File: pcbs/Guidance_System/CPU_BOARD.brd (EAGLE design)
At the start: 100 x 80 mm, 16 parts, among them J1 22-27-2081-08, J2 22-27-2021-02, J3 22-05-7048-04, J4 22-05-7048-04, J5 22-27-2081-08, J6 22-27-2021-02, J7 22-27-2081-08

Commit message: * Added Driver board. Many corrections and refinements.
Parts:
- removed S1: 2P2T, switch:2P2T
- added J10, J11, J12, J13, J14: 22-27-2081-08, con-molex:6410-08
- added J15, J16: 22-27-2041-04, con-molex:6410-04
- added J17, J8, J9: 22-27-2021-02, con-molex:6410-02
- J3, J4: value 22-05-7048-04 -> 22-27-2041-04; device con-molex:7395-04 -> con-molex:6410-04
- moved J7 48.1 mm to (88.9, 33.0), turned to 0 degrees
- moved R6 28.4 mm to (92.7, 29.2)
- moved J5 19.1 mm to (59.7, 40.6), turned to 270 degrees
- moved J2 18.2 mm to (66.0, 66.0)
- moved J1 18.0 mm to (59.7, 62.2)
- moved R2 16.7 mm to (80.0, 62.2)
- moved R3 16.7 mm to (80.0, 59.7)
- moved U$1 16.7 mm to (77.5, 57.1)
- moved R4 15.9 mm to (95.2, 39.4), turned to 180 degrees
- moved LED1 13.1 mm to (66.0, 31.8)
- moved J6 11.7 mm to (72.4, 31.8), turned to 0 degrees
- moved R1 11.5 mm to (90.2, 62.2), turned to 90 degrees
- moved J3 10.2 mm to (95.2, 61.0)
- moved J4 9.67 mm to (95.2, 47.0)
- moved R5 8.89 mm to (66.0, 50.8)
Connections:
- new net N$19: J13.5, J13.6
- new net N$24: J1.1, J3.2, J4.2, J9.1, U$1.23
- new net N$26: J10.8, J14.8
- new net N$27: J10.7, J14.5
- new net N$28: J13.7, J14.6
- new net N$29: J13.8, J14.7
- new net N$31: J11.8, J12.8, J17.2
- new net N$32: J10.3, J11.2, J12.2, J13.3, J14.1
- new net N$33: J11.1, J12.1, J14.2
- new net N$34: J11.7, J12.7, J17.1
- new net N$35: J10.1, J13.1, J14.4
- new net N$37: J11.6, J15.1
- new net N$38: J11.5, J15.2
- new net N$39: J11.4, J15.3
- new net N$40: J11.3, J15.4
- new net N$41: J12.6, J16.1
- new net N$42: J12.5, J16.2
- new net N$43: J12.4, J16.3
- new net N$44: J12.3, J16.4
- net N$4: now also J10.5, J10.6; no longer J1.1, J3.2, J4.2, U$1.23
- net N$5: now also J8.2; no longer S1.3.2
- net VCC: now also J8.1, J9.2; no longer S1.3.1
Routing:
- net N$33: track 0.00 -> 129.5 mm, vias 0 -> 2
- net N$4: track 102.9 -> 2.54 mm
- net N$24: track 0.00 -> 99.1 mm
- net N$32: track 0.00 -> 98.3 mm, vias 0 -> 2
- net N$31: track 0.00 -> 47.0 mm
- net N$35: track 0.00 -> 46.6 mm
- net N$34: track 0.00 -> 41.9 mm, vias 0 -> 2
- net N$13: track 16.1 -> 56.7 mm
- net N$29: track 0.00 -> 36.8 mm
- net N$3: track 191.2 -> 156.1 mm
- net N$27: track 0.00 -> 33.0 mm, vias 0 -> 1
- net N$8: track 12.5 -> 42.4 mm
- net N$14: track 19.7 -> 47.5 mm
- net N$7: track 8.15 -> 35.6 mm
- net N$22: track 11.4 -> 35.3 mm
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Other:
- board size 100 x 80 mm -> 100 x 55.9 mm
- board text added: "S1 Driver"
- board text added: "S2 Driver"

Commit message: * Committing latest version before major shrinkage of boards
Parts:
- moved R6 6.84 mm to (86.4, 31.8)
- moved R5 4.58 mm to (62.2, 53.3)
- moved LED1 4.58 mm to (62.2, 34.3)
- moved J8 4.58 mm to (86.4, 72.4)
- moved J9 4.58 mm to (92.7, 72.4)
- moved J2 4.58 mm to (62.2, 68.6)
- moved J3 4.58 mm to (91.4, 63.5)
- moved J4 4.58 mm to (91.4, 49.5)
- moved J6 4.58 mm to (68.6, 34.3)
- moved J7 4.58 mm to (85.1, 35.6)
- moved R1 4.58 mm to (86.4, 64.8)
- moved R2 4.58 mm to (76.2, 64.8)
- moved R3 4.58 mm to (76.2, 62.2)
- moved R4 4.58 mm to (91.4, 41.9)
- moved U$1 4.58 mm to (73.7, 59.7)
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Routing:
- net N$3: track 156.1 -> 152.3 mm
- net N$27: track 33.0 -> 29.2 mm
- net N$29: track 36.8 -> 33.0 mm
- net N$17: track 46.5 -> 43.6 mm
- net N$24: track 99.1 -> 96.5 mm
- net N$22: track 35.3 -> 33.4 mm
- net N$26: track 15.2 -> 14.0 mm
- net N$33: track 129.5 -> 128.3 mm
- net N$32: track 98.3 -> 97.0 mm
- net N$21: track 32.8 -> 31.7 mm
- net GND: track 79.8 -> 78.8 mm
- net N$35: track 46.6 -> 47.5 mm
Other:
- board size 100 x 55.9 mm -> 100 x 49.5 mm

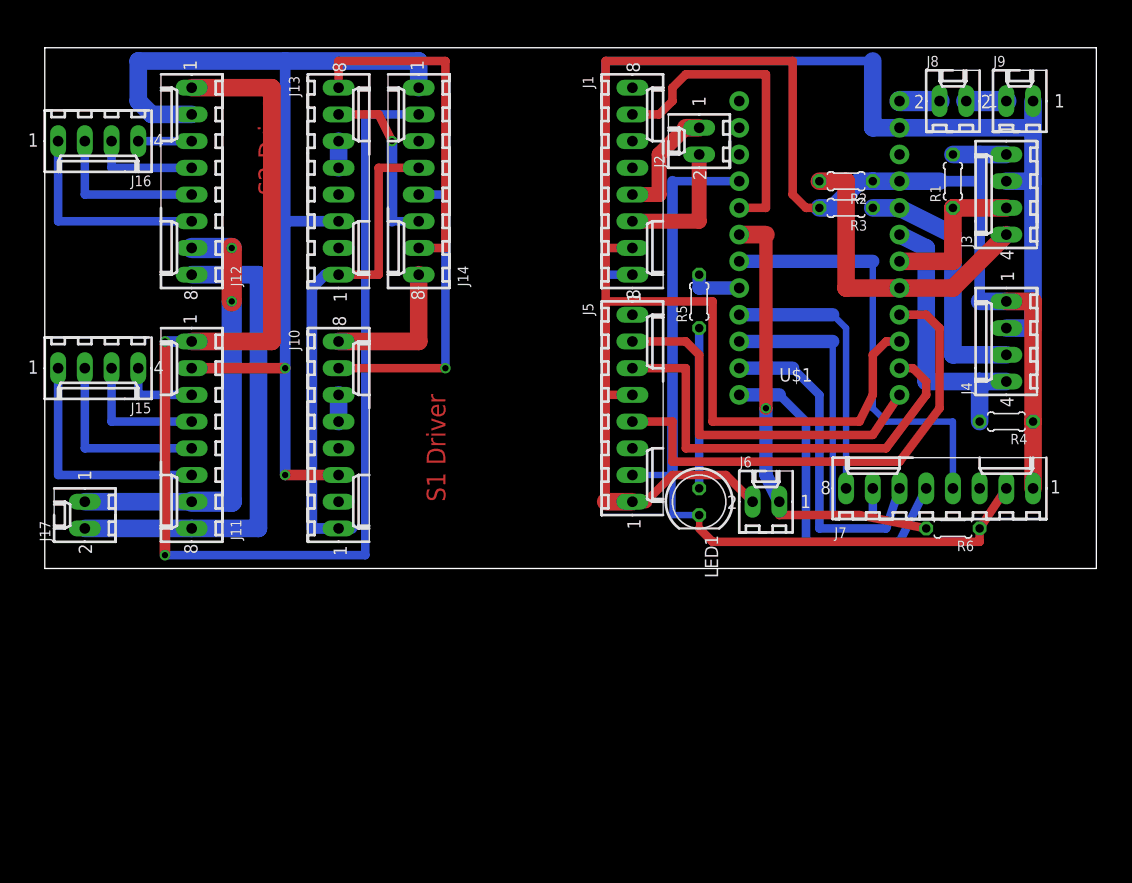
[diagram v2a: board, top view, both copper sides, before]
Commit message: * Made boards a lot smaller a much better layout!
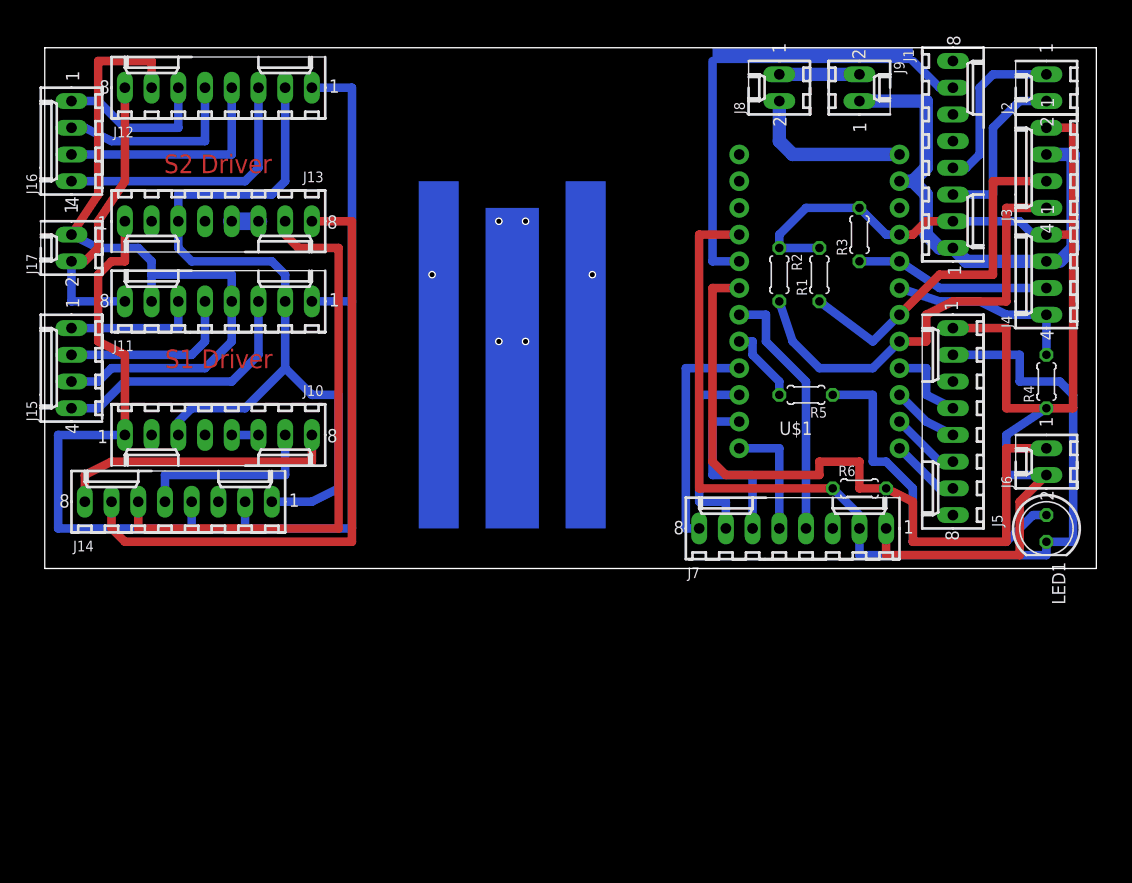
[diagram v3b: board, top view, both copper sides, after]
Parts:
- moved J14 38.1 mm to (12.7, 34.3), turned to 0 degrees
- moved J2 33.4 mm to (95.2, 73.7)
- moved LED1 33.1 mm to (95.2, 31.8)
- moved J1 30.6 mm to (86.4, 67.3)
- moved J5 30.5 mm to (86.4, 41.9), turned to 90 degrees
- moved J6 26.9 mm to (95.2, 38.1), turned to 90 degrees
- moved J17 25.4 mm to (2.54, 58.4)
- moved J8 16.6 mm to (69.8, 73.7), turned to 90 degrees
- moved R1 15.5 mm to (73.7, 55.9)
- moved J9 15.3 mm to (77.5, 73.7), turned to 270 degrees
- moved J7 14.5 mm to (71.1, 31.8)
- moved R5 13.5 mm to (72.4, 44.5), turned to 180 degrees
- moved J11 13.0 mm to (16.5, 53.3), turned to 0 degrees
- moved J13 12.0 mm to (16.5, 61.0), turned to 180 degrees
- moved J10 11.4 mm to (16.5, 40.6), turned to 180 degrees
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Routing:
- net N$33: track 128.3 -> 62.2 mm, vias 2 -> 0
- net N$13: track 56.7 -> 6.43 mm
- net N$24: track 96.5 -> 48.4 mm
- net N$14: track 47.5 -> 7.92 mm
- net N$28: track 16.8 -> 55.1 mm, vias 1 -> 0
- net N$8: track 42.4 -> 6.66 mm
- net N$3: track 152.3 -> 121.8 mm, vias 0 -> 2
- net N$7: track 35.6 -> 6.66 mm
- net N$29: track 33.0 -> 60.2 mm
- net N$17: track 43.6 -> 68.1 mm, vias 1 -> 0
- net N$22: track 33.4 -> 11.4 mm
- net N$44: track 5.08 -> 25.9 mm
- net GND: track 78.8 -> 98.1 mm
- net N$11: track 15.2 -> 34.4 mm
- net N$31: track 47.0 -> 28.0 mm
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
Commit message: * Reducing width of PCBs to 46mm * Adding in places to drill holes * Adding in text to assist in identifying connectors and what they are for.
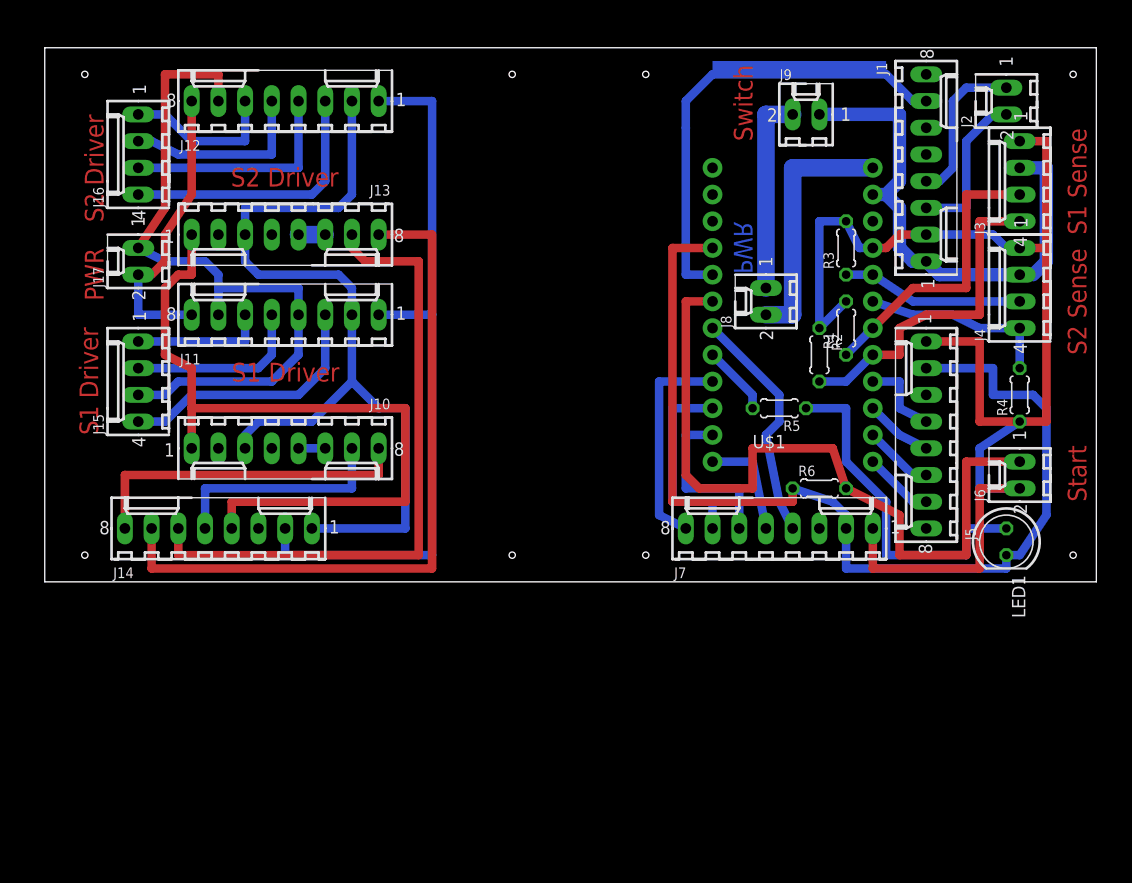
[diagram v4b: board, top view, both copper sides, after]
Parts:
- moved J8 20.4 mm to (68.6, 53.3)
- moved R2 8.52 mm to (73.7, 48.3)
- moved J15 6.48 mm to (8.89, 45.7)
- moved J17 6.48 mm to (8.89, 57.1)
- moved J16 6.48 mm to (8.89, 67.3)
- moved J10 6.48 mm to (22.9, 39.4)
- moved J11 6.48 mm to (22.9, 52.1)
- moved J13 6.48 mm to (22.9, 59.7)
- moved J12 6.48 mm to (22.9, 72.4)
- moved R1 5.68 mm to (76.2, 50.8)
- moved J9 5.68 mm to (72.4, 71.1), turned to 0 degrees
- moved J14 4.58 mm to (16.5, 31.8)
- moved LED1 4.02 mm to (91.4, 30.5)
- moved J2 4.02 mm to (91.4, 72.4)
- moved R6 3.81 mm to (73.7, 35.6)
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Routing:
- net N$35: track 54.2 -> 71.9 mm
- net VCC: track 7.62 -> 19.1 mm
- net N$12: track 42.0 -> 31.8 mm
- net N$5: track 15.8 -> 24.1 mm
- net N$33: track 62.2 -> 69.8 mm
- net N$29: track 60.2 -> 67.3 mm
- net N$11: track 34.4 -> 28.0 mm
- net N$28: track 55.1 -> 61.5 mm
- net N$26: track 27.0 -> 31.7 mm
- net N$32: track 80.0 -> 84.7 mm
- net N$27: track 17.8 -> 21.6 mm
- net N$3: track 121.8 -> 125.1 mm
- net N$17: track 68.1 -> 71.2 mm
- net N$23: track 24.4 -> 22.6 mm
- net N$6: track 45.5 -> 44.0 mm
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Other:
- board size 100 x 49.5 mm -> 100 x 50.8 mm
- board text added: "PWR"
- board text added: "S1 Sense"
- board text added: "S2 Sense"
- board text added: "Start"
- board text added: "Switch"

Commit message: * Reduced width of PCB (bringing holes closer) * Also moved holes closer in longitudinal direction in effort to improve strength * Swapped Start switch and LED around to make better set-up inside airframe.
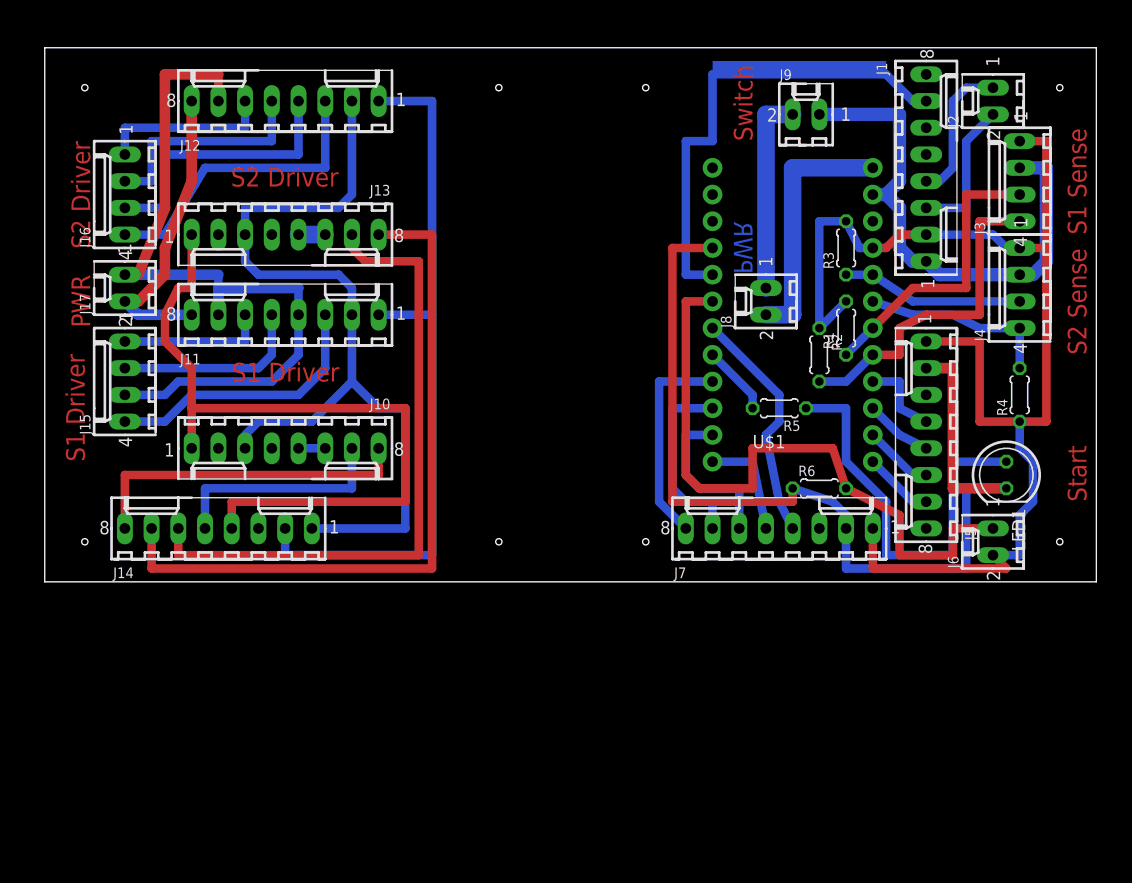
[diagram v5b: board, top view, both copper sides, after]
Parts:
- moved J6 6.84 mm to (90.2, 30.5)
- moved LED1 6.35 mm to (91.4, 36.8)
- moved J16 4.02 mm to (7.62, 63.5)
- moved J17 2.84 mm to (7.62, 54.6)
- moved J15 1.27 mm to (7.62, 45.7)
- moved J2 1.27 mm to (90.2, 72.4)
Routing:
- net N$17: track 71.2 -> 62.3 mm
- net N$16: track 33.3 -> 39.7 mm
- net GND: track 98.5 -> 93.4 mm
- net N$43: track 21.6 -> 26.7 mm
- net N$34: track 47.3 -> 51.3 mm
- net N$42: track 18.1 -> 21.6 mm
- net N$44: track 25.9 -> 29.0 mm
- net N$3: track 125.1 -> 122.1 mm
- net N$6: track 44.0 -> 45.5 mm
- net N$41: track 15.0 -> 16.5 mm
- net N$40: track 25.0 -> 26.2 mm
- net N$38: track 17.0 -> 18.3 mm
- net N$39: track 20.6 -> 21.9 mm
- net N$37: track 12.7 -> 14.0 mm
- net N$2: track 15.0 -> 13.8 mm
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
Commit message: * Flipped power/switch around * Adding holes /tracks for step control pins on drivers * Adding text in and around pcb components to help us identify different parts
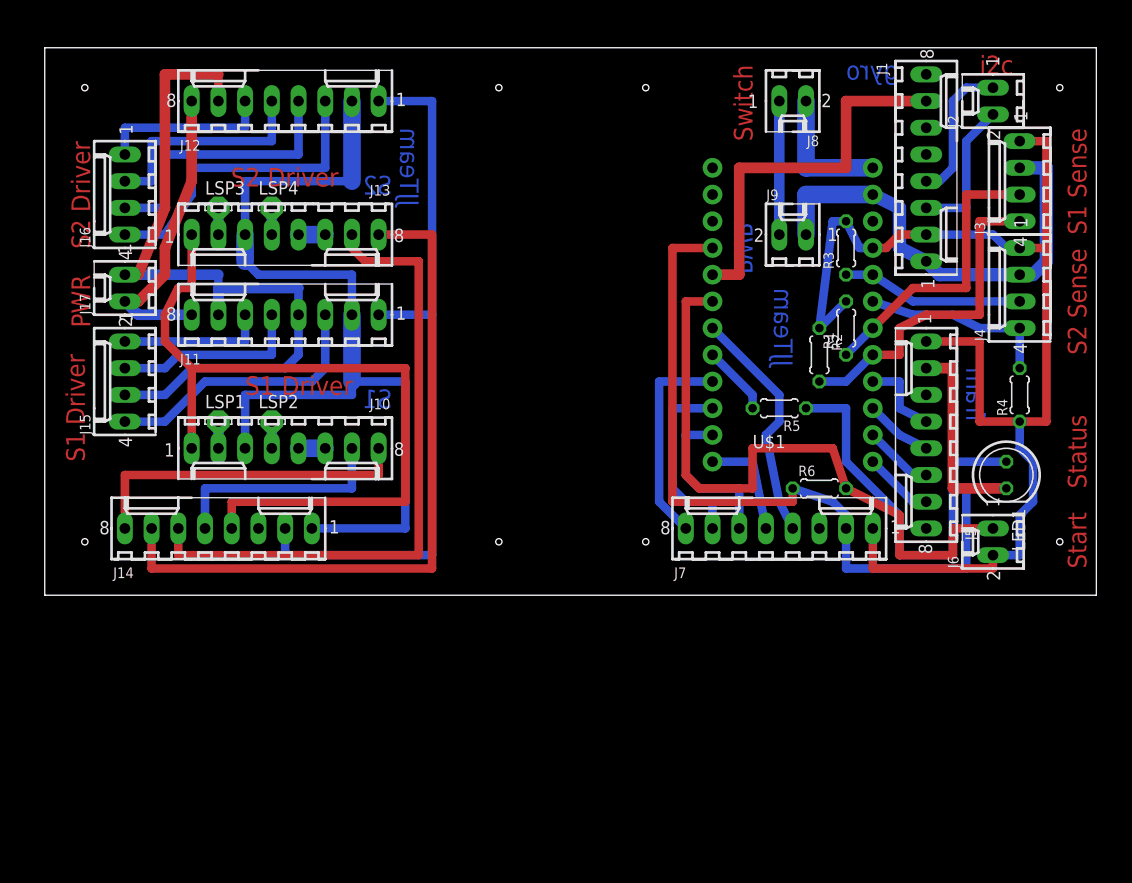
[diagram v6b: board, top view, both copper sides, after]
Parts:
- added LSP1, LSP2, LSP3, LSP4: LSP10, solpad:LSP10
- moved J8 19.2 mm to (71.1, 72.4), turned to 180 degrees
- moved J9 11.5 mm to (71.1, 59.7)
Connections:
- new net N$25: J10.4, LSP2.MP
- new net N$30: J10.2, LSP1.MP
- new net N$36: J13.4, LSP4.MP
- new net N$45: J13.2, LSP3.MP
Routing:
- net N$5: track 24.1 -> 12.7 mm
- net N$6: track 45.5 -> 36.8 mm
- net VCC: track 19.1 -> 12.7 mm
- net N$24: track 49.6 -> 43.6 mm
- net N$32: track 84.7 -> 90.7 mm
- net N$35: track 71.2 -> 75.0 mm
- net N$3: track 122.1 -> 119.1 mm
- net N$45: track 0.00 -> 2.54 mm
- net N$36: track 0.00 -> 2.54 mm
- net N$30: track 0.00 -> 2.54 mm
- net N$25: track 0.00 -> 2.54 mm
- net N$44: track 29.0 -> 30.0 mm
- net N$16: track 39.7 -> 38.9 mm
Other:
- board size 100 x 50.8 mm -> 100 x 52.1 mm
- board text added: "JJTeam"
- board text added: "S1"
- board text added: "S2"
- board text added: "Status"
- board text added: "fram"
- board text added: "gyro"
- board text added: "i2c"
